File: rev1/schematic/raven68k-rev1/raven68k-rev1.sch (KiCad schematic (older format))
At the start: 14 parts

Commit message: update schematic for rev1
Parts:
- removed C? (x2): C_Small, symbol Device:C_Small
- X?: value CXO_DIP14 -> CLOCK
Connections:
- net labels added: A1, A10, A11, A12, A13, A14, A15, A16, A17, A18, A19, A2, A20, A21, A22, A23, A3, A4, A5, A6, A7, A8, A9, D0, D1, D10, D11, D12, D13, D14, D15, D2, D3, D4, D5, D6, D7, D8, D9, FC0, FC1, FC2, IPL0, IPL1, IPL2, SQU, ~IDE_CE, ~RTC_CE, ~RTC_CS, ~RTC_IRQ
- wire segments 180 -> 172
- no-connect marks 3 -> 11

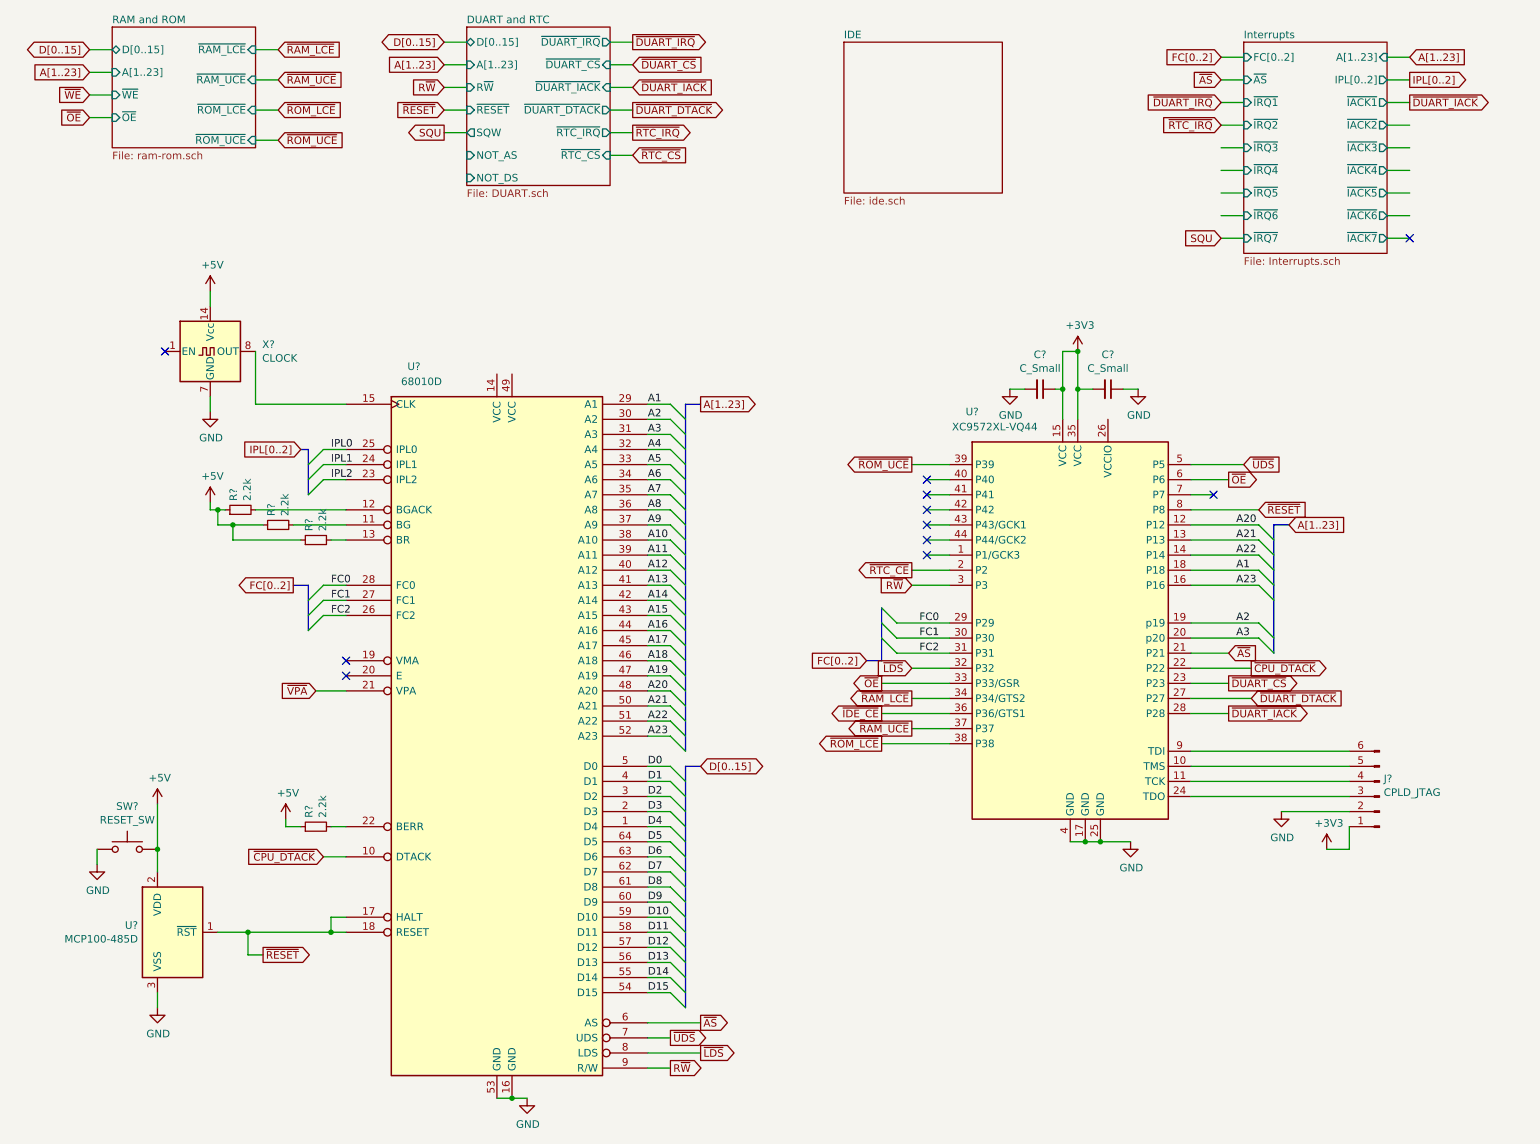
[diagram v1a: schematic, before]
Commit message: added buffers
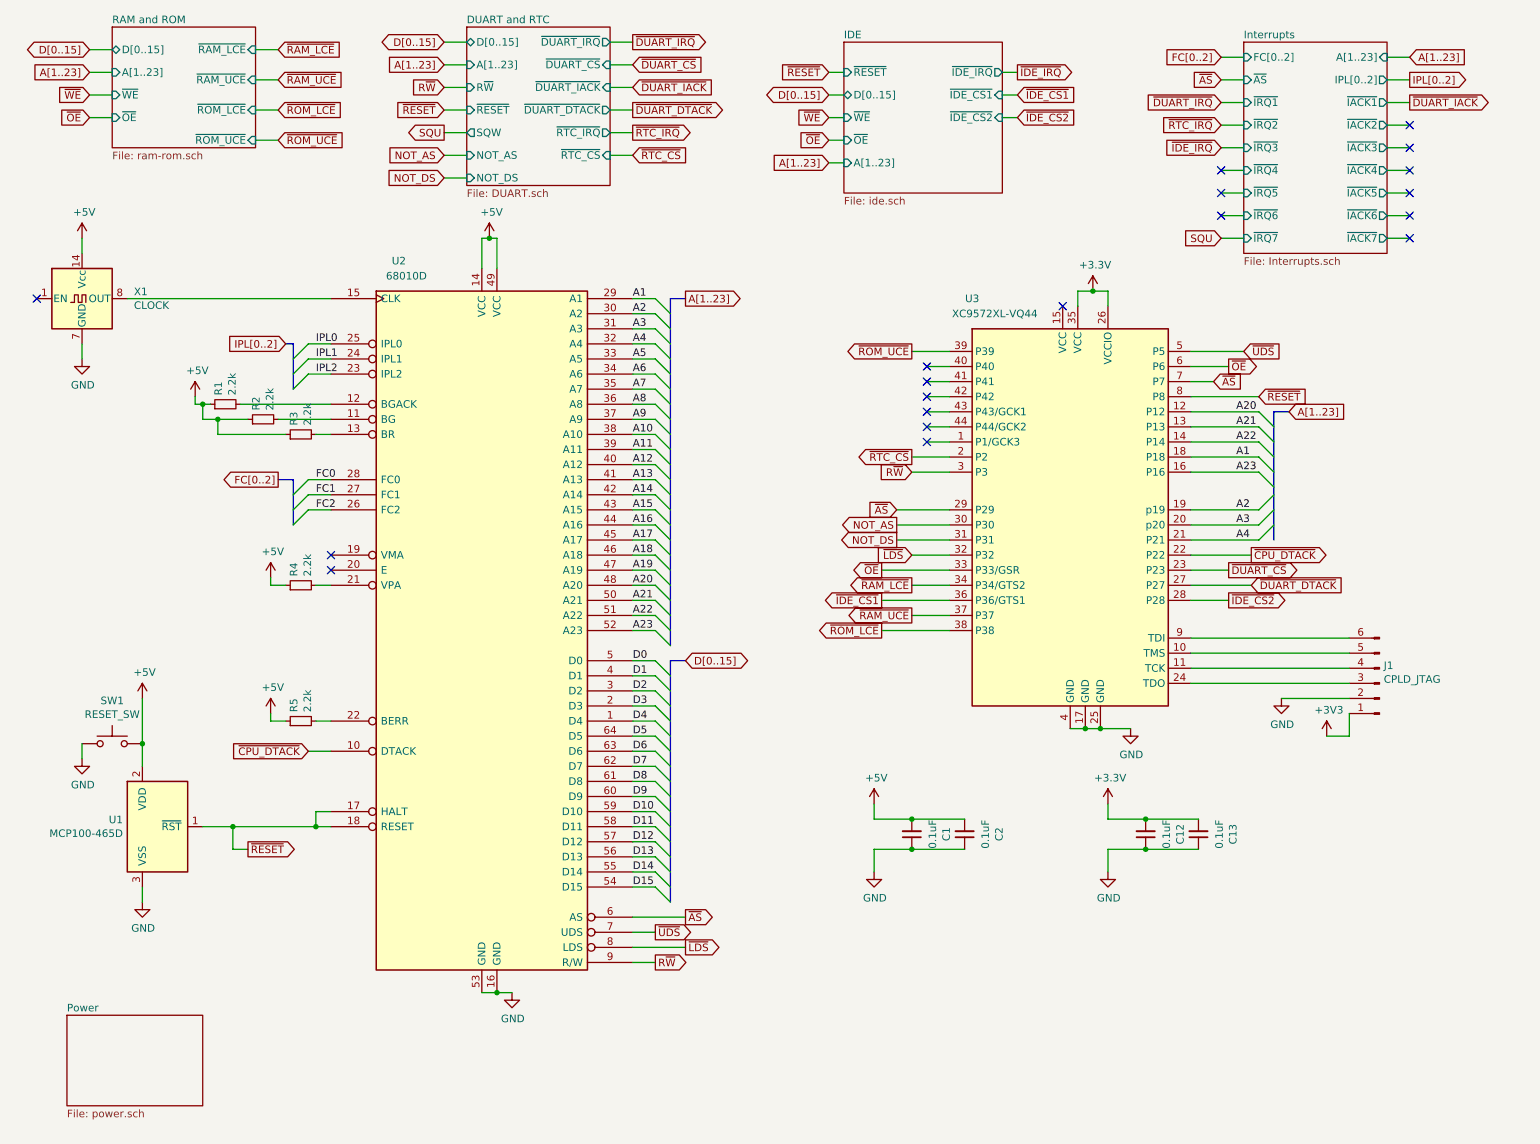
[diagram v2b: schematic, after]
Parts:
- removed C? (x2): C_Small, symbol Device:C_Small
- added C1, C12, C13, C2: 0.1uF, symbol Device:C_Small
- added R4: 2.2k, symbol Device:R_Small
- J1: renamed from J?; footprint (none) -> Connector_PinHeader_2.54mm:PinHeader_1x06_P2.54mm_Vertical
- U1: renamed from U?; value MCP100-485D -> MCP100-465D; footprint (none) -> Package_TO_SOT_THT:TO-92L_Inline_Wide
- U2: renamed from U?; footprint (none) -> Package_DIP:DIP-64_W25.4mm_Socket
- gave numbers to parts that had none: 7
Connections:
- net labels added: +3.3V, NOT_AS, NOT_DS, ~IDE_CS1, ~IDE_CS2, ~IDE_IRQ
- net labels removed: ~IDE_CE, ~RTC_CE, ~VPA
- wire segments 172 -> 194
- no-connect marks 11 -> 19
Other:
- moved on the sheet: J1, R1, R2, R3, R5, SW1, U1, U2, U3, X1

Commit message: upgrade to KiCad 6, first shot at layout
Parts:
- C1, C2: footprint (none) -> Capacitor_SMD:C_1206_3216Metric_Pad1.33x1.80mm_HandSolder
- C3: renamed from C12; footprint (none) -> Capacitor_SMD:C_1206_3216Metric_Pad1.33x1.80mm_HandSolder
- C4: renamed from C13; footprint (none) -> Capacitor_SMD:C_1206_3216Metric_Pad1.33x1.80mm_HandSolder
- U1: footprint Package_TO_SOT_THT:TO-92L_Inline_Wide -> (none)
- U2: footprint Package_DIP:DIP-64_W25.4mm_Socket -> Package_DIP:DIP-64_W25.4mm_Socket_LongPads
- X1: footprint Oscillator:Oscillator_DIP-14 -> Oscillator:Oscillator_DIP-14_LargePads
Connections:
- net FC0: now also U3.40 (P40)
- net FC1: now also U3.41 (P41)
- net FC2: now also U3.42 (P42)
- net ~DUART_IACK: now also U3.43 (P43/GCK1)
- net IPL0 renamed ~IPL0
- net IPL1 renamed ~IPL1
- net IPL2 renamed ~IPL2
- no-connect marks 19 -> 6
